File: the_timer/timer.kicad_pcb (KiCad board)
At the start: 2 copper layers, 18 x 37.5 mm, 23 parts, among them J1 AVR-ISP-6, J2 Conn_01x04_Socket, J3 Conn_01x02_Socket, Q1 2N7002, Q2 2N7002, Q3 2N7002, U1 ATtiny48-A, U2 TPS61033, U3 MC3416, U4 W25Q128JVS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

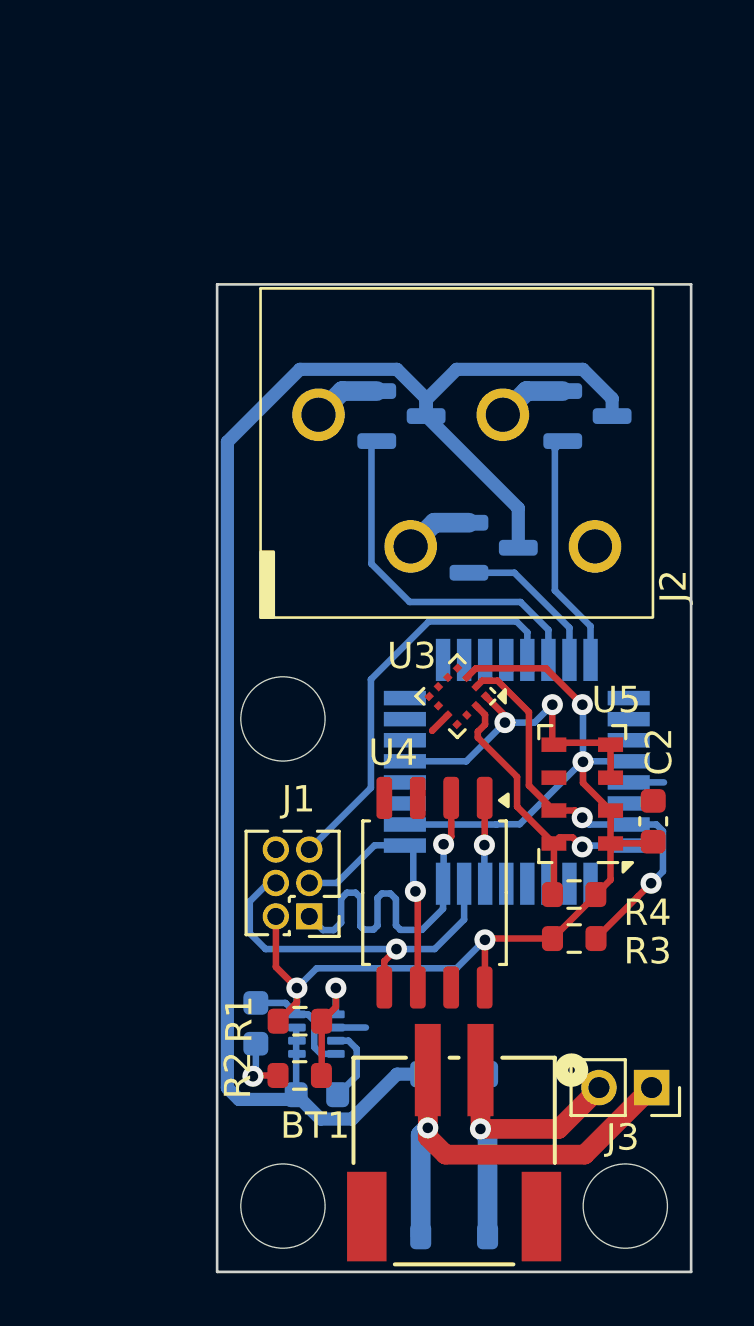
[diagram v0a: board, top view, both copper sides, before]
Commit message: Replaced Timer mosfets
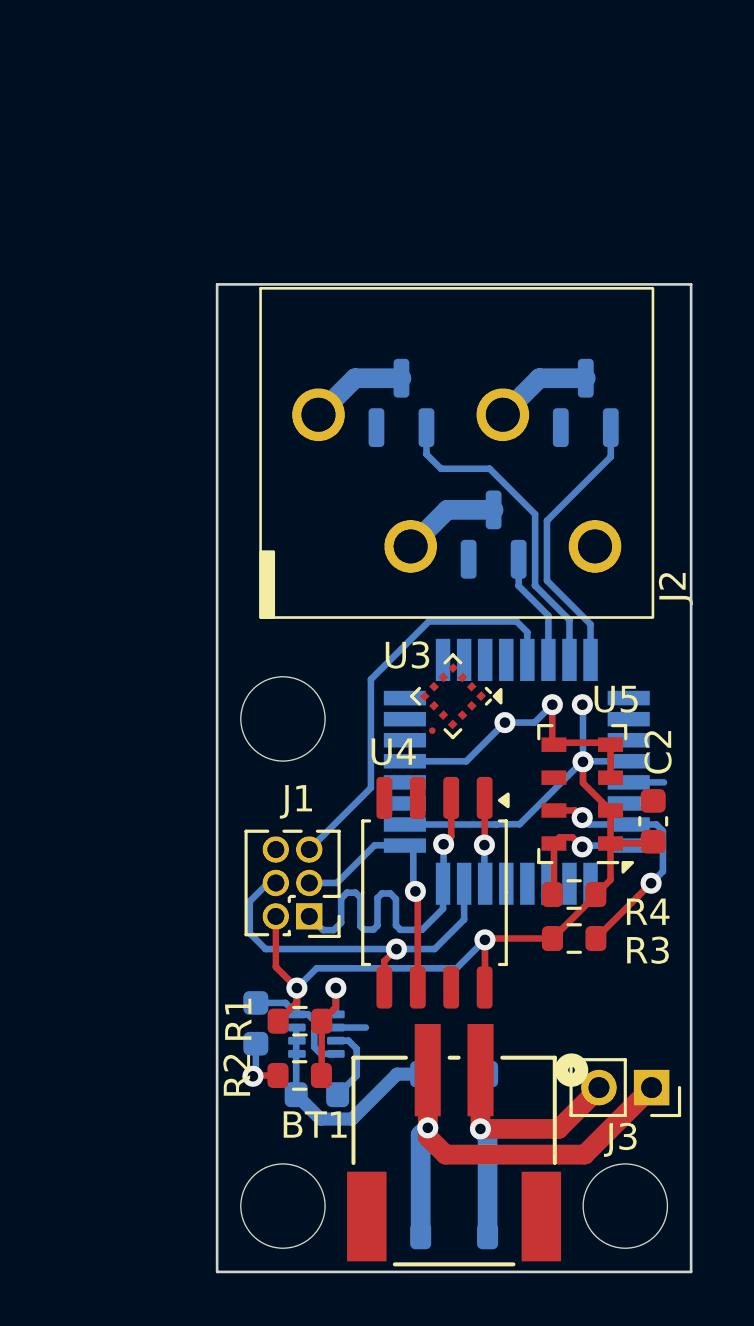
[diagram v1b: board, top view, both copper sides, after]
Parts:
- Q1, Q2, Q3: value 2N7002 -> AS2312
- moved Q3 0.50 mm to (220.0, 75.8), turned to 90 degrees
- moved Q1 0.50 mm to (213.0, 75.8), turned to 90 degrees
- moved Q2 0.50 mm to (216.5, 80.8), turned to 90 degrees
- moved U3 0.17 mm to (215.0, 86.9)
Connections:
- net t2 renamed T_{3}
- J2 pad 1: c0 -> C_{1}
- J2 pad 2: c1 -> C_{2}
- J2 pad 3: c2 -> C_{3}
- J2 pad 4: GND -> V_{B}
- Q1 pad 1: t0 -> T_{1}
- Q1 pad 2: c0 -> GND
- Q1 pad 3: V_{B} -> C_{1}
- Q2 pad 1: t1 -> T_{2}
- Q2 pad 2: c1 -> GND
- Q2 pad 3: V_{B} -> C_{2}
- Q3 pad 2: c2 -> GND
- Q3 pad 3: V_{B} -> C_{3}
- U1 pad 30: t0 -> T_{2}
- U1 pad 31: t1 -> T_{1}
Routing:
- net V_{B}: track 61.3 -> 8.38 mm
- net t0: track 13.6 -> 0.00 mm
- net T_{1}: track 0.00 -> 12.2 mm
- net SDA: track 16.3 -> 9.60 mm
- net SCL: track 11.8 -> 5.08 mm
- net t1: track 5.90 -> 0.00 mm
- net V_{CC}: track 48.8 -> 43.7 mm
- net T_{2}: track 0.00 -> 4.29 mm
- net C_{3}: track 0.00 -> 3.72 mm
- net C_{2}: track 0.00 -> 3.72 mm
- net C_{1}: track 0.00 -> 3.72 mm
- net c2: track 2.65 -> 0.00 mm
- net c1: track 2.59 -> 0.00 mm
- net c0: track 2.59 -> 0.00 mm
- net GND: track 18.4 -> 16.2 mm
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
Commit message: Generated Screamer and Timer BOMs
Both Screamer and Timer have been bumped to V0.1.
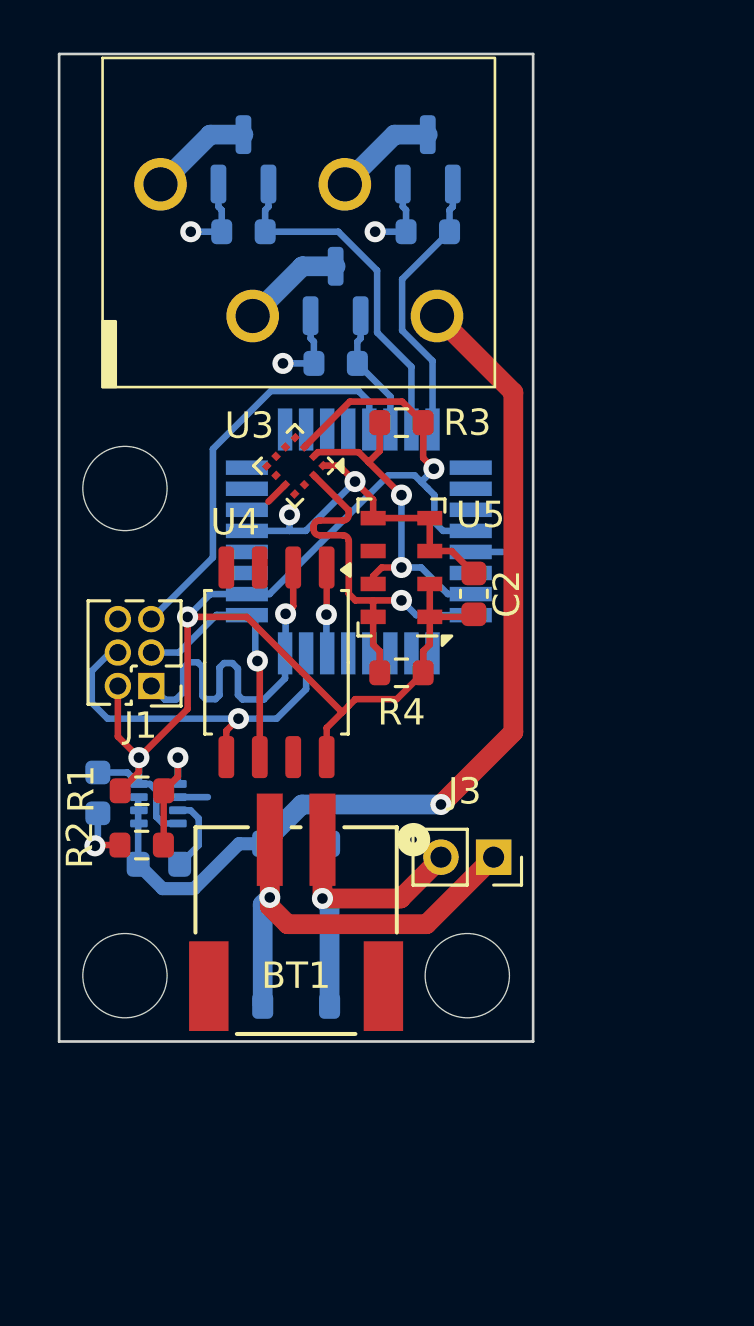
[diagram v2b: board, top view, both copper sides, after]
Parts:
- added R5: 10k, Resistor_SMD:R_0603_1608Metric, B.Cu at (207.0, 69.2)
- added R6: 10k, Resistor_SMD:R_0603_1608Metric, B.Cu at (210.5, 74.2)
- added R7: 10k, Resistor_SMD:R_0603_1608Metric, B.Cu at (214.0, 69.2)
- J2: value Conn_01x04_Socket -> 1-2834019-4
- J3: value Conn_01x02_Socket -> 2RS1-02-G
- U1: value ATtiny48-A -> ATTINY88-AU
- U2: value TPS61033 -> TPS61033DRLR
- moved R3 20.7 mm to (213.0, 76.5), turned to 180 degrees
- moved Q1 11.0 mm to (207.0, 66.5)
- moved Q2 11.0 mm to (210.5, 71.5)
- moved Q3 11.0 mm to (214.0, 66.5)
- moved U5 11.0 mm to (213.0, 82.0)
- moved C2 11.0 mm to (215.8, 83.0)
- moved R4 10.7 mm to (213.0, 86.0)
- moved BT1 10.6 mm to (208.0, 92.3)
- moved C3 10.6 mm to (201.5, 90.6)
- moved D1 10.6 mm to (209.0, 95.6)
- moved H1 10.6 mm to (202.5, 79.0)
- moved H2 10.6 mm to (215.5, 97.5)
- moved H3 10.6 mm to (202.5, 97.5)
- moved J1 10.6 mm to (203.5, 86.5)
- moved J2 10.6 mm to (201.7, 75.2)
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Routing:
- net V_{B}: track 8.38 -> 36.7 mm, vias 0 -> 1
- net V_{CC}: track 43.7 -> 57.0 mm, vias 4 -> 3
- net GND: track 16.2 -> 28.8 mm, vias 3 -> 6
- net SCL: track 5.08 -> 15.1 mm
- net SDA: track 9.60 -> 13.1 mm
- net T_{1}: track 12.2 -> 13.3 mm
- net T_{2}: track 4.29 -> 4.89 mm
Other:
- board text added: "V0.1.2"

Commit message: Fixed custom symbol file paths
In addition to fixing all the file paths I also updated some symbols on the Timer and Screamer, updated the board characteristic tables, added missing 3D models to some components, and did a bit of other file stuff.
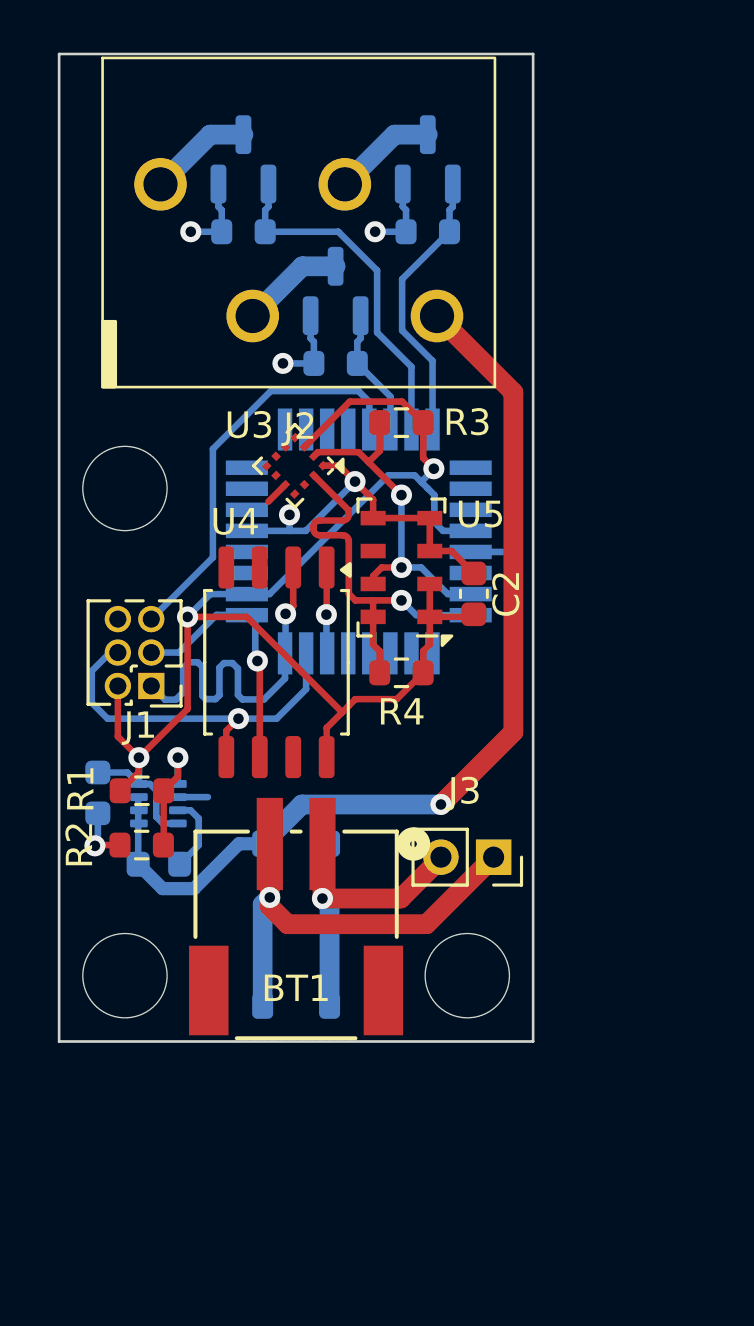
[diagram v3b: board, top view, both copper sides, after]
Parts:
- J2: footprint locals:TE_1-2834019-4 -> locals_but_working_PLEASE:TE_1-2834019-4
- moved BT1 7.73 mm to (209.0, 100.0)
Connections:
- net Net-(BT1-+) renamed /BT-
- net Net-(BT1--) renamed /BT+
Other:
- board text added: "0.0000 mm / 0.0000 mm"
- board text added: "0.3000 mm"
- board text added: "1.6000 mm"
- board text added: "18.0000 mm x 37.5000 mm"
- board text added: "2"
- board text added: "BOARD CHARACTERISTICS"
- board text added: "Board Thickness:"
- board text added: "Board overall dimensions:"
- board text added: "Castellated pads:"
- board text added: "Copper Finish:"
- board text added: "Copper Layer Count:"
- board text added: "Edge card connectors:"
- board text added: "Impedance Control:"
- board text added: "Min hole diameter:"
- board text added: "Min track/spacing:"
- board text added: "No"
- board text added: "None"
- board text added: "Plated Board Edge:"

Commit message: Added automatic revision label to PCBs
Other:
- board text added: "${REVISION}"
- board text removed: "V0.1.2"
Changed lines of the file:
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@@
 		)
 		(property "Value" "MC3416"
-			(at -10.737971 -6.297339 225)
+			(at -10.737971 -6.297339 -135)
 			(layer "F.Fab")
 			(effects
@@
 		(layer "Edge.Cuts")
 	)
-	(gr_text "V0.1.2"
-		(at 200.5 75 270)
+	(gr_text "${REVISION}"
+		(at 217.5 86.5 90)
 		(layer "B.SilkS")
 		(effects

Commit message: Tweaked timer traces a bit
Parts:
- moved R3 1.30 mm to (212.3, 77.6)
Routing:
- net SDA: track 13.1 -> 11.4 mm
- net V_{CC}: track 57.0 -> 56.1 mm, vias 3 -> 4
- net GND: vias 6 -> 7

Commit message: Accelerometer code nearing completion
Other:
- board text added: "+X"
- board text added: "+Z"
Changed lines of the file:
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@@
 		(at 201.65 75.15)
 		(property "Reference" "J2"
-			(at 7.5 1.5 0)
+			(at 2.22 0.84 0)
 			(unlocked yes)
 			(layer "F.SilkS")
@@
 		(tags "Kionix LGA NoLead")
 		(property "Reference" "U3"
-			(at 0.141421 2.305168 180)
+			(at 0.299966 2.251581 180)
 			(layer "F.SilkS")
 			(effects
@@
 		)
 	)
+	(gr_text "+X"
+		(at 205.49 78.58 0)
+		(layer "F.SilkS")
+		(effects
+			(font
+				(size 0.7 0.7)
+				(thickness 0.15)
+			)
+			(justify left bottom)
+		)
+	)
+	(gr_text "+Z"
+		(at 208.12 76.31 0)
+		(layer "F.SilkS")
+		(effects
+			(font
+				(size 0.7 0.7)
+				(thickness 0.15)
+				(bold yes)
+			)
+			(justify left bottom)
+		)
+	)
